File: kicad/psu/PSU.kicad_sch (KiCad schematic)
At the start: 47 parts, among them J1 B2B-PH-K-S, J2 Conn_01x09_Pin, U1 BQ21040DBVR, U2 RT4812GJ8F, U3 AP3445LW6-7, U4 AP3445LW6-7

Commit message: Update PSU.kicad_sch
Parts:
- removed J2: Conn_01x09_Pin, symbol Connector:Conn_01x09_Pin
- added J2: Conn_01x07_Pin, symbol Connector:Conn_01x07_Pin
- C11, C12: footprint Capacitor_SMD:C_0402_1005Metric -> Capacitor_SMD:C_0805_2012Metric
- R1, R10, R11, R12, R13, R14, R15, R2, R3, R4, R5, R6, R7, R8, R9: footprint Resistor_SMD:R_0402_1005Metric -> Resistor_SMD:R_0805_2012Metric
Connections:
- net 1.8V: now also J2.1 (Pin_1)
- net 3.3V: now also J2.2 (Pin_2)
- net 5V: now also J2.3 (Pin_3)
- net GND: now also J2.4 (Pin_4)
- net PG_1.8: now also J2.5 (Pin_5)
- net PG_3.3: now also J2.6 (Pin_6)
- net at R8.2, R9.1: now also J2.7 (Pin_7)
- net D+: no longer names the net of USB-C1.A6 (DP1)
- net D+: no longer USB-C1.B6 (DP2)
- net D-: no longer names the net of USB-C1.A7 (DN1)
- net D-: no longer USB-C1.B7 (DN2)
- no-connect marks 2 -> 6
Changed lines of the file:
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@@
 	)
 	(junction
-		(at 152.4 190.5)
-		(diameter 0)
-		(color 0 0 0 0)
-	)
-	(junction
 		(at 77.47 59.69)
 		(diameter 0)
@@
 	)
 	(junction
-		(at 95.25 106.68)
+		(at 129.54 190.5)
 		(diameter 0)
 		(color 0 0 0 0)
 	)
 	(junction
-		(at 129.54 190.5)
+		(at 95.25 106.68)
 		(diameter 0)
 		(color 0 0 0 0)
 	)
 	(no_connect
+		(at 33.02 36.83)
+	)
+	(no_connect
 		(at 73.66 41.91)
 	)
@@
 		(at 33.02 39.37)
 	)
+	(no_connect
+		(at 33.02 34.29)
+	)
+	(no_connect
+		(at 73.66 36.83)
+	)
+	(no_connect
+		(at 73.66 39.37)
+	)
 	(wire
 		(pts
@@
 	(wire
 		(pts
-			(xy 152.4 190.5) (xy 153.67 190.5)
-		)
-		(stroke
-			(width 0)
-			(type default)
-		)
-	)
-	(wire
-		(pts
 			(xy 184.15 144.78) (xy 204.47 144.78)
 		)
@@
 	(wire
 		(pts
+			(xy 129.54 190.5) (xy 152.4 190.5)
+		)
+		(stroke
+			(width 0)
+			(type default)
+		)
+	)
+	(wire
+		(pts
 			(xy 187.96 124.46) (xy 200.66 124.46)
 		)
@@
 	(wire
 		(pts
-			(xy 129.54 190.5) (xy 152.4 190.5)
-		)
-		(stroke
-			(width 0)
-			(type default)
-		)
-	)
-	(wire
-		(pts
 			(xy 184.15 142.24) (xy 223.52 142.24)
 		)
@@
 		)
 	)
-	(global_label "D+"
-		(shape input)
-		(at 73.66 36.83 0)
-		(fields_autoplaced yes)
-		(effects
-			(font
-				(size 1.27 1.27)
-			)
-			(justify left)
-		)
-		(property "Intersheetrefs" "${INTERSHEET_REFS}"
-			(at 79.4876 36.83 0)
-			(effects
-				(font
-					(size 1.27 1.27)
-				)
-				(justify left)
-				(hide yes)
-			)
-		)
-	)
-	(global_label "D-"
-		(shape input)
-		(at 73.66 39.37 0)
-		(fields_autoplaced yes)
-		(effects
-			(font
-				(size 1.27 1.27)
-			)
-			(justify left)
-		)
-		(property "Intersheetrefs" "${INTERSHEET_REFS}"
-			(at 79.4876 39.37 0)
-			(effects
-				(font
-					(size 1.27 1.27)
-				)
-				(justify left)
-				(hide yes)
-			)
-		)
-	)
-	(global_label "D+"
-		(shape input)
-		(at 152.4 193.04 180)
-		(fields_autoplaced yes)
-		(effects
-			(font
-				(size 1.27 1.27)
-			)
-			(justify right)
-		)
-		(property "Intersheetrefs" "${INTERSHEET_REFS}"
-			(at 146.5724 193.04 0)
-			(effects
-				(font
-					(size 1.27 1.27)
-				)
-				(justify right)
-				(hide yes)
-			)
-		)
-	)
-	(global_label "D-"
-		(shape input)
-		(at 33.02 36.83 180)
-		(fields_autoplaced yes)
-		(effects
-			(font
-				(size 1.27 1.27)
-			)
-			(justify right)
-		)
-		(property "Intersheetrefs" "${INTERSHEET_REFS}"
-			(at 27.1924 36.83 0)
-			(effects
-				(font
-					(size 1.27 1.27)
-				)
-				(justify right)
-				(hide yes)
-			)
-		)
-	)
-	(global_label "D-"
-		(shape input)
-		(at 152.4 195.58 180)
-		(fields_autoplaced yes)
-		(effects
-			(font
-				(size 1.27 1.27)
-			)
-			(justify right)
-		)
-		(property "Intersheetrefs" "${INTERSHEET_REFS}"
-			(at 146.5724 195.58 0)
-			(effects
-				(font
-					(size 1.27 1.27)
-				)
-				(justify right)
-				(hide yes)
-			)
-		)
-	)
-	(global_label "D+"
-		(shape input)
-		(at 33.02 34.29 180)
-		(fields_autoplaced yes)
-		(effects
-			(font
-				(size 1.27 1.27)
-			)
-			(justify right)
-		)
-		(property "Intersheetrefs" "${INTERSHEET_REFS}"
-			(at 27.1924 34.29 0)
-			(effects
-				(font
-					(size 1.27 1.27)
-				)
-				(justify right)
-				(hide yes)
-			)
-		)
-	)
 	(symbol
 		(lib_id "Device:C")
@@
 			)
 		)
-		(property "Footprint" "Capacitor_SMD:C_0402_1005Metric"
+		(property "Footprint" "Capacitor_SMD:C_0805_2012Metric"
 			(at 199.39 110.7948 0)
 			(effects
@@
 			)
 		)
-		(property "Footprint" "Resistor_SMD:R_0402_1005Metric"
+		(property "Footprint" "Resistor_SMD:R_0805_2012Metric"
 			(at 195.58 104.902 90)
 			(effects
@@
 	)
 	(symbol
-		(lib_id "Connector:Conn_01x09_Pin")
-		(at 157.48 185.42 180)
+		(lib_id "Connector:Conn_01x07_Pin")
+		(at 157.48 182.88 0)
+		(mirror y)
 		(unit 1)
 		(exclude_from_sim no)
@@
 		(fields_autoplaced yes)
 		(property "Reference" "J2"
-			(at 158.75 184.1499 0)
+			(at 158.75 181.6099 0)
 			(effects
 				(font
@@
 			)
 		)
-		(property "Value" "Conn_01x09_Pin"
-			(at 158.75 186.6899 0)
+		(property "Value" "Conn_01x07_Pin"
+			(at 158.75 184.1499 0)
 			(effects
 				(font
@@
 		)
 		(property "Footprint" ""
-			(at 157.48 185.42 0)
+			(at 157.48 182.88 0)
 			(effects
 				(font
@@
 		)
 		(property "Datasheet" "~"
-			(at 157.48 185.42 0)
+			(at 157.48 182.88 0)
 			(effects
 				(font
@@
 			)
 		)
-		(property "Description" "Generic connector, single row, 01x09, script generated"
-			(at 157.48 185.42 0)
+		(property "Description" "Generic connector, single row, 01x07, script generated"
+			(at 157.48 182.88 0)
 			(effects
 				(font
@@
 			)
 		)
-		(pin "4"
-		)
-		(pin "9"
-		)
-		(pin "7"
+		(pin "1"
 		)
 		(pin "6"
 		)
-		(pin "3"
-		)
-		(pin "2"
+		(pin "4"
 		)
-		(pin "8"
+		(pin "7"
 		)
-		(pin "1"
+		(pin "2"
 		)
 		(pin "5"
 		)
+		(pin "3"
+		)
 		(instances
 			(project ""
@@
 			)
 		)
-		(property "Footprint" "Capacitor_SMD:C_0402_1005Metric"
+		(property "Footprint" "Capacitor_SMD:C_0805_2012Metric"
 			(at 201.93 46.0248 0)
 			(effects
@@
 			)
 		)
-		(property "Footprint" "Resistor_SMD:R_0402_1005Metric"
+		(property "Footprint" "Resistor_SMD:R_0805_2012Metric"
 			(at 95.25 84.328 90)
 			(effects
@@
 			)
 		)
-		(property "Footprint" "Resistor_SMD:R_0402_1005Metric"
+		(property "Footprint" "Resistor_SMD:R_0805_2012Metric"
 			(at 173.99 163.068 90)
 			(effects
@@
 			)
 		)
-		(property "Footprint" "Resistor_SMD:R_0402_1005Metric"
+		(property "Footprint" "Resistor_SMD:R_0805_2012Metric"
 			(at 29.21 29.972 90)
 			(effects
@@
 			)
 		)
-		(property "Footprint" "Resistor_SMD:R_0402_1005Metric"
+		(property "Footprint" "Resistor_SMD:R_0805_2012Metric"
 			(at 194.31 163.068 90)
 			(effects
@@
 			)
 		)
-		(property "Footprint" "Resistor_SMD:R_0402_1005Metric"
+		(property "Footprint" "Resistor_SMD:R_0805_2012Metric"
 			(at 21.082 104.14 90)
 			(effects
@@
 			)
 		)
-		(property "Footprint" "Resistor_SMD:R_0402_1005Metric"
+		(property "Footprint" "Resistor_SMD:R_0805_2012Metric"
 			(at 131.318 185.42 90)
 			(effects
@@
 			)
 		)
-		(property "Footprint" "Resistor_SMD:R_0402_1005Metric"
+		(property "Footprint" "Resistor_SMD:R_0805_2012Metric"
 			(at 82.55 36.068 90)
 			(effects
@@
 			)
 		)
-		(property "Footprint" "Resistor_SMD:R_0402_1005Metric"
+		(property "Footprint" "Resistor_SMD:R_0805_2012Metric"
 			(at 198.12 40.132 90)
 			(effects
@@
 			)
 		)
-		(property "Footprint" "Resistor_SMD:R_0402_1005Metric"
+		(property "Footprint" "Resistor_SMD:R_0805_2012Metric"
 			(at 213.36 43.688 90)
 			(effects
@@
 			)
 		)
-		(property "Footprint" "Resistor_SMD:R_0402_1005Metric"
+		(property "Footprint" "Resistor_SMD:R_0805_2012Metric"
 			(at 116.84 192.278 90)
 			(effects
@@
 			)
 		)
-		(property "Footprint" "Resistor_SMD:R_0402_1005Metric"
+		(property "Footprint" "Resistor_SMD:R_0805_2012Metric"
 			(at 94.742 153.67 90)
 			(effects
@@
 			)
 		)
-		(property "Footprint" "Resistor_SMD:R_0402_1005Metric"
+		(property "Footprint" "Resistor_SMD:R_0805_2012Metric"
 			(at 210.82 108.458 90)
 			(effects
@@
 			)
 		)
-		(property "Footprint" "Resistor_SMD:R_0402_1005Metric"
+		(property "Footprint" "Resistor_SMD:R_0805_2012Metric"
 			(at 94.742 163.83 90)
 			(effects
@@
 			)
 		)
-		(property "Footprint" "Resistor_SMD:R_0402_1005Metric"
+		(property "Footprint" "Resistor_SMD:R_0805_2012Metric"
 			(at 29.972 104.14 90)
 			(effects

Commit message: Update PSU.kicad_sch
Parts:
- removed J2: Conn_01x07_Pin, symbol Connector:Conn_01x07_Pin
- removed R2, R4: 22K, Resistor_SMD:R_0805_2012Metric, symbol Device:R
- removed USB-C1: USB4105-GF-A, USB4105-GF-A-120:GCT_USB4105-GF-A-120, symbol USB4105-GF-A-120:USB4105-GF-A-120
- added J2: Conn_01x08_Pin, symbol Connector:Conn_01x08_Pin
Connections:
- net 1.8V: now also J2.1 (Pin_1)
- net 3.3V: now also J2.2 (Pin_2)
- net 5V: now also J2.3 (Pin_3)
- net GND: now also J2.4 (Pin_4)
- net PG_1.8: now also J2.5 (Pin_5)
- net PG_3.3: now also J2.6 (Pin_6)
- net Vcharger: now also J2.8 (Pin_8)
- net at R8.2, R9.1: now also J2.7 (Pin_7)
- no-connect marks 6 -> 0
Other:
- moved on the sheet: R8, R9

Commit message: PSU diodes and footprints
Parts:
- added D2, D3, D4: D, Diode_SMD:D_0805_2012Metric, symbol Device:D
- added D5: D, symbol Device:D
- F1, F2, F3, F4: footprint (none) -> Fuse:Fuse_0805_2012Metric
- J1: footprint B2B-PH-K-S:JST_B2B-PH-K-S -> Connector_JST:JST_PH_B2B-PH-K_1x02_P2.00mm_Vertical
- J2: footprint (none) -> Connector_PinHeader_2.54mm:PinHeader_1x08_P2.54mm_Vertical
- L1: footprint SPM6530T_1R5M100:IND_SPM6530T-1R5M100 -> PSAT_Library:IND_SPM6530T-1R5M100
- U1: footprint BQ21040DBVR:SOT95P280X145-6N -> PSAT_Library:BQ21040DBVR
- U2: footprint RT4812GJ8F:SOT65P279X100-8N -> PSAT_Library:RT4812GJ8F
- U3, U4: footprint footprints:SOT26_AP3445_DIO -> PSAT_Library:SOT26_AP3445_DIO-L
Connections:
- net 1.8V: now also D2.2 (A); no longer J2.1 (Pin_1)
- net 3.3V: now also D3.2 (A); no longer J2.2 (Pin_2)
- net 5V: now also D4.2 (A); no longer J2.3 (Pin_3)
- net Vcharger: now also D5.1 (K); no longer J2.8 (Pin_8)
- new net: D2.1 (K), J2.1 (Pin_1)
- new net: D5.2 (A), J2.8 (Pin_8)
- new net: D3.1 (K), J2.2 (Pin_2)
- new net: D4.1 (K), J2.3 (Pin_3)

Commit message: PSU Routing
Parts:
- D5: footprint (none) -> Diode_SMD:D_0805_2012Metric
- renumbered JP3 to EN_1.8, JP2 to EN_3.3, JP1 to EN_5
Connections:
- net +1.8V is gone; now on net 1.8V: F2.2
- net +3.3V is gone; now on net 3.3V: F3.2
- net +5V is gone; now on net 5V: F4.2
- net PG_1.8: now also J2.6 (Pin_6); no longer J2.5 (Pin_5)
- net PG_3.3: now also J2.5 (Pin_5); no longer J2.6 (Pin_6)

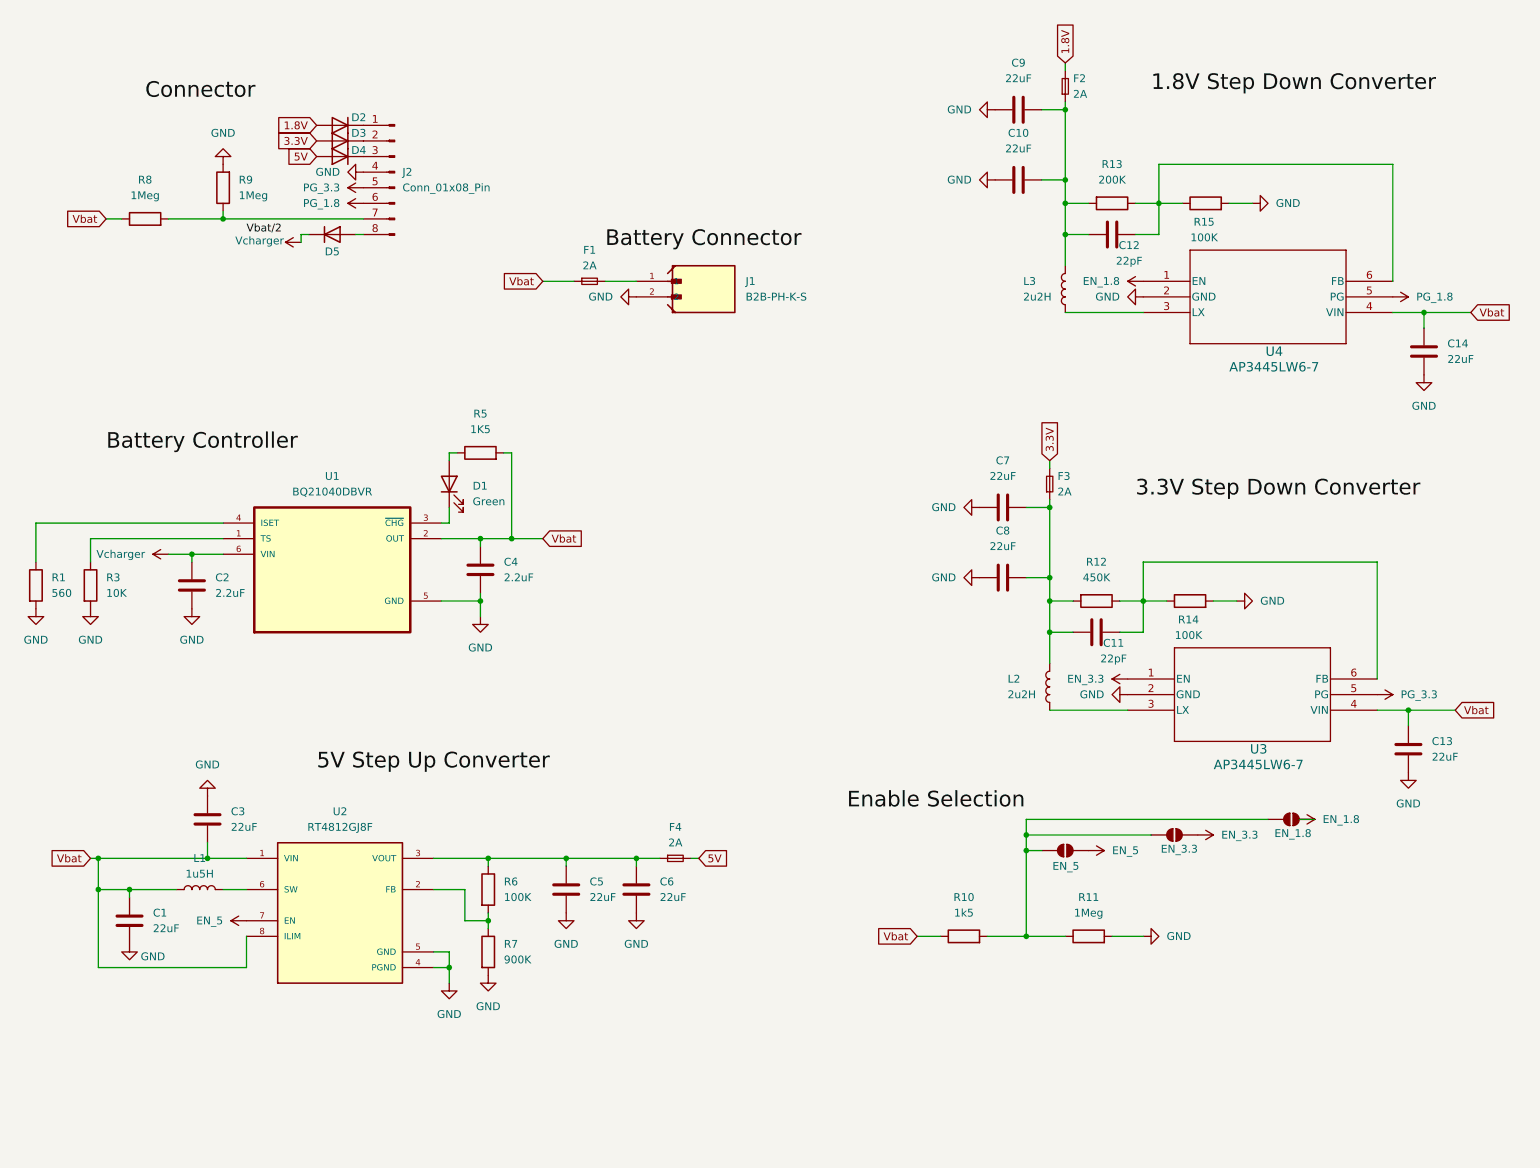
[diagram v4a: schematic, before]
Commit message: Added Test points and non fused 3.3V
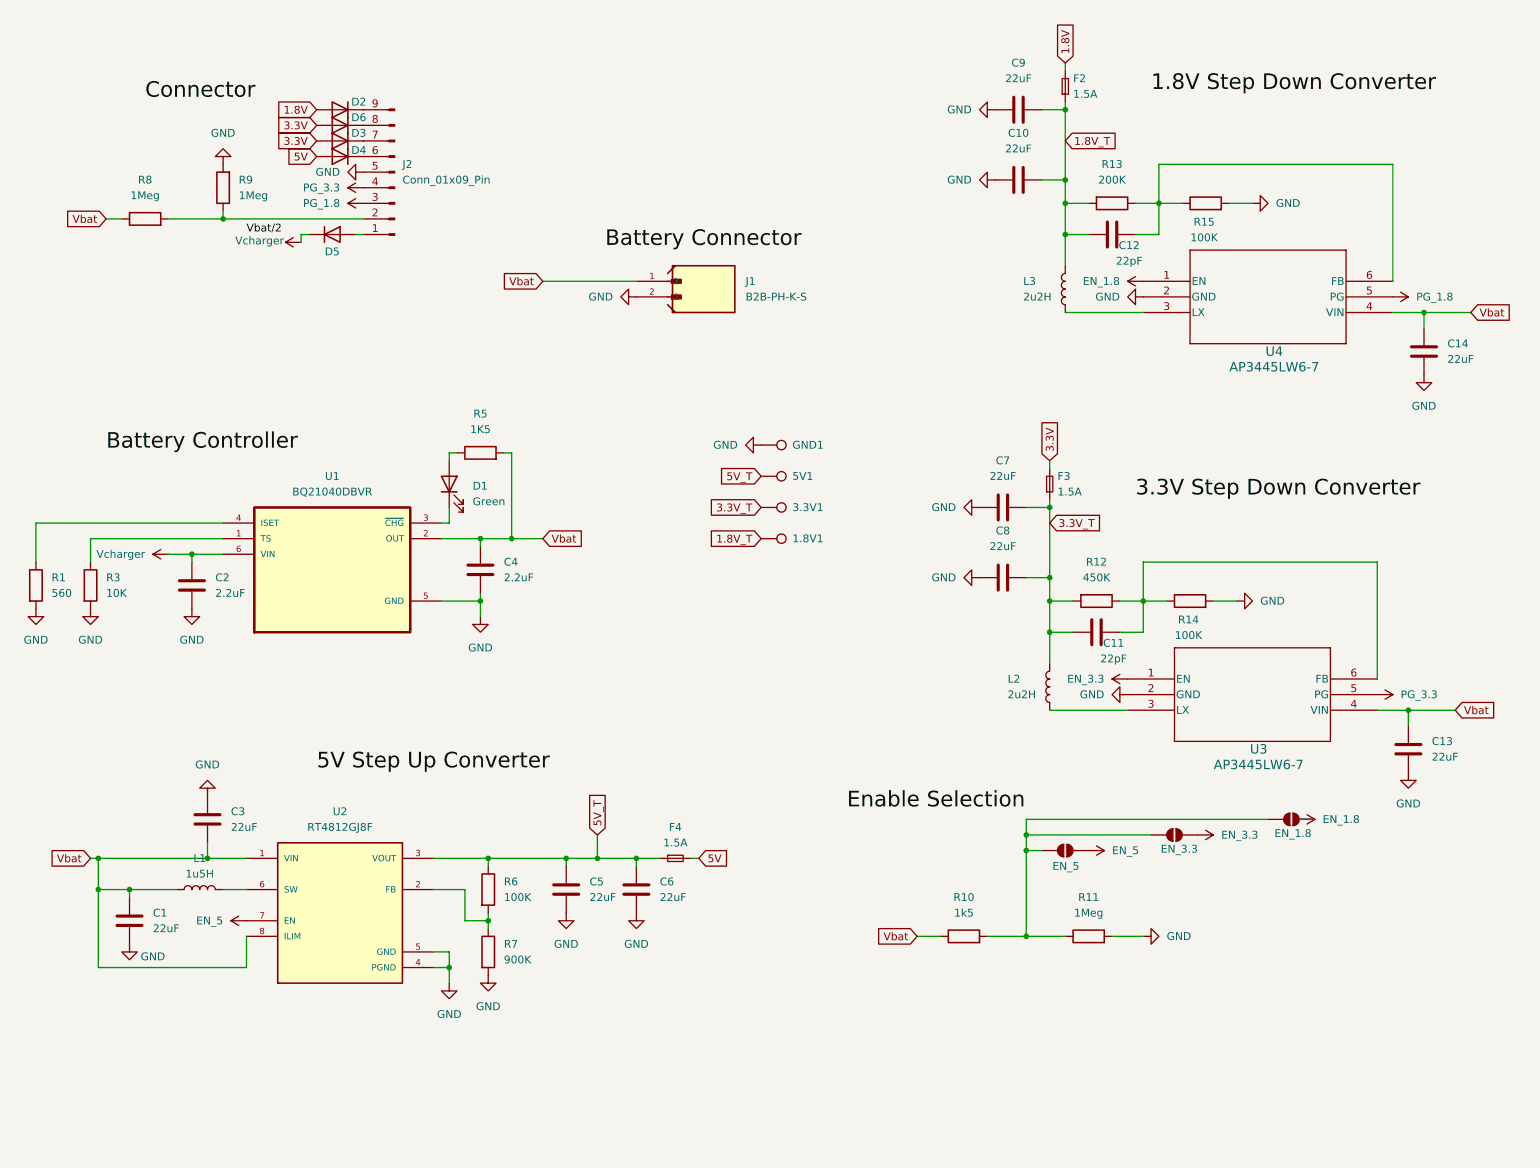
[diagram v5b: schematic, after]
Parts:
- removed F1: 2A, Fuse:Fuse_0805_2012Metric, symbol Device:Fuse_Small
- removed J2: Conn_01x08_Pin, Connector_PinHeader_2.54mm:PinHeader_1x08_P2.54mm_Vertical, symbol Connector:Conn_01x08_Pin
- added 1.8V1, 3.3V1, 5V1, GND1: TestPoint, TestPoint:TestPoint_Pad_1.5x1.5mm, symbol Connector:TestPoint
- added D6: D, Diode_SMD:D_0805_2012Metric, symbol Device:D
- added J2: Conn_01x09_Pin, Connector_PinSocket_2.54mm:PinSocket_1x09_P2.54mm_Vertical, symbol Connector:Conn_01x09_Pin
- F2, F3, F4: value 2A -> 1.5A
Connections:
- net 3.3V: now also D6.2 (A)
- net GND: now also GND1.1, J2.5 (Pin_5)
- net PG_1.8: now also J2.3 (Pin_3)
- net PG_3.3: now also J2.4 (Pin_4)
- net Vbat: now also J1.1
- net 3.3V_T: now reaches C11.1, C7.2, C8.2, F3.1, L2.1, R12.2
- net 3.3V_T: now also 3.3V1.1
- net 1.8V_T: now reaches C10.2, C12.1, C9.2, F2.1, L3.1, R13.2
- net 1.8V_T: now also 1.8V1.1
- net at D2.1 (K): now also J2.9 (Pin_9)
- net 5V_T: now reaches C5.2, C6.1, F4.1, R6.1, U2.3 (VOUT)
- net 5V_T: now also 5V1.1
- net at D5.2 (A): now also J2.1 (Pin_1)
- net at R8.2, R9.1: now also J2.2 (Pin_2)
- net at D3.1 (K): now also J2.7 (Pin_7)
- net at D4.1 (K): now also J2.6 (Pin_6)
- new net: D6.1 (K), J2.8 (Pin_8)
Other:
- moved on the sheet: D2

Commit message: PSU Rev 2
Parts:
- removed D2, D3, D4, D5, D6: D, Diode_SMD:D_0805_2012Metric, symbol Device:D
- added D2, D3, D4, D5, D6: D_Schottky, Diode_SMD:D_0805_2012Metric, symbol Device:D_Schottky
- added J3: *, PSAT_Library:GCT_USB4125-GF-A_REVA2, symbol PSAT_Library:USB4125-GF-A_REVA2
- added R16: 22K, Resistor_SMD:R_0805_2012Metric, symbol Device:R
- added R2, R4: 1Meg, Resistor_SMD:R_0805_2012Metric, symbol Device:R
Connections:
- net 1.8V: now also D2.2 (A)
- net 3.3V: now also D4.2 (A)
- net 3.3V_T: now also D3.2 (A)
- net 5V: now also D6.2 (A)
- net EN_1.8: now also R4.1
- net EN_3.3: now also R2.1
- net EN_5: now also R11.1
- net GND: now also J3.A12 (GND), J3.B12 (GND), J3.S1 (SHIELD), J3.S2 (SHIELD), J3.S3 (SHIELD), J3.S4 (SHIELD), R16.2, R2.2, R4.2
- net Vcharger: now also D5.1 (K), J3.A9 (VBUS), J3.B9 (VBUS)
- net at EN_1.8.2 (B), EN_3.3.2 (B), EN_5.2 (B)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: no longer R11.1
- net at J2.8 (Pin_8): now also D3.1 (K)
- net at J2.9 (Pin_9): now also D2.1 (K)
- net at J2.1 (Pin_1): now also D5.2 (A)
- net at J2.7 (Pin_7): now also D4.1 (K)
- net at J2.6 (Pin_6): now also D6.1 (K)
- new net: J3.A5 (CC1), J3.B5 (CC2), R16.1
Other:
- moved on the sheet: 1.8V1, 3.3V1, 5V1, EN_3.3, EN_5, GND1, J1, R11
